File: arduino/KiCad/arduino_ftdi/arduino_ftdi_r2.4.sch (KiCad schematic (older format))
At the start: 19 parts, among them J1 RJ45, J10 9V-12V, J11 3V3 & 5V, J12 9V-12V, J13 3V3 & 5V, J2 IN/OUT, J3 DTR/TX/RX, J4 Power output 3V3, J5 NC, J6 DTR-FTDI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

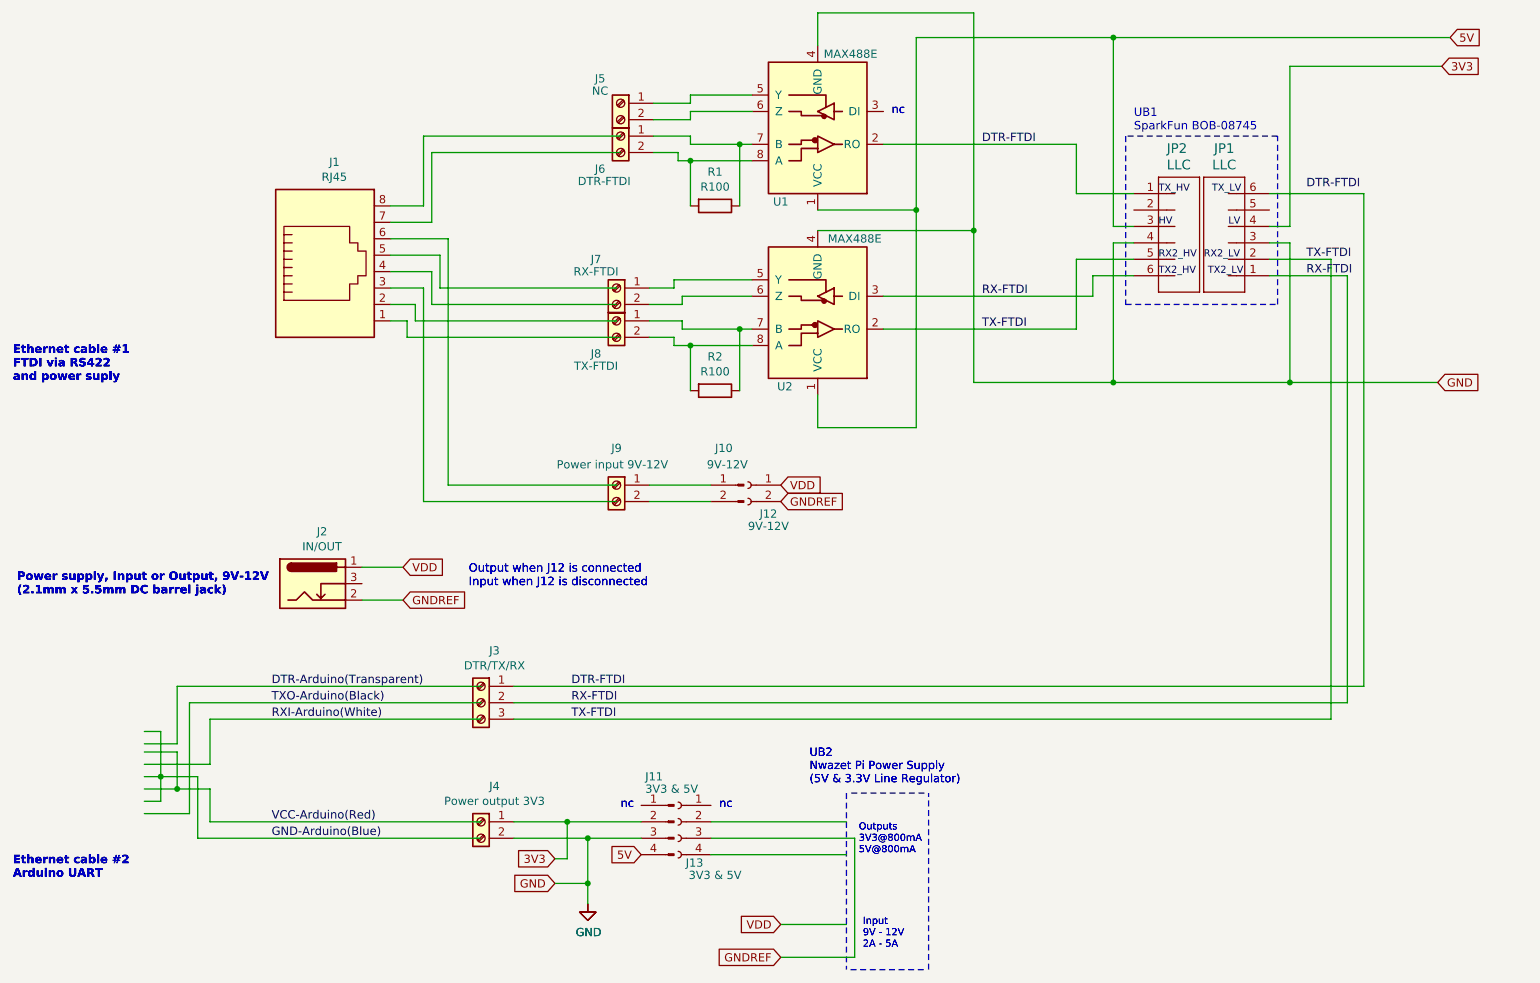
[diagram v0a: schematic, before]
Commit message: Update FTDI interface schematics
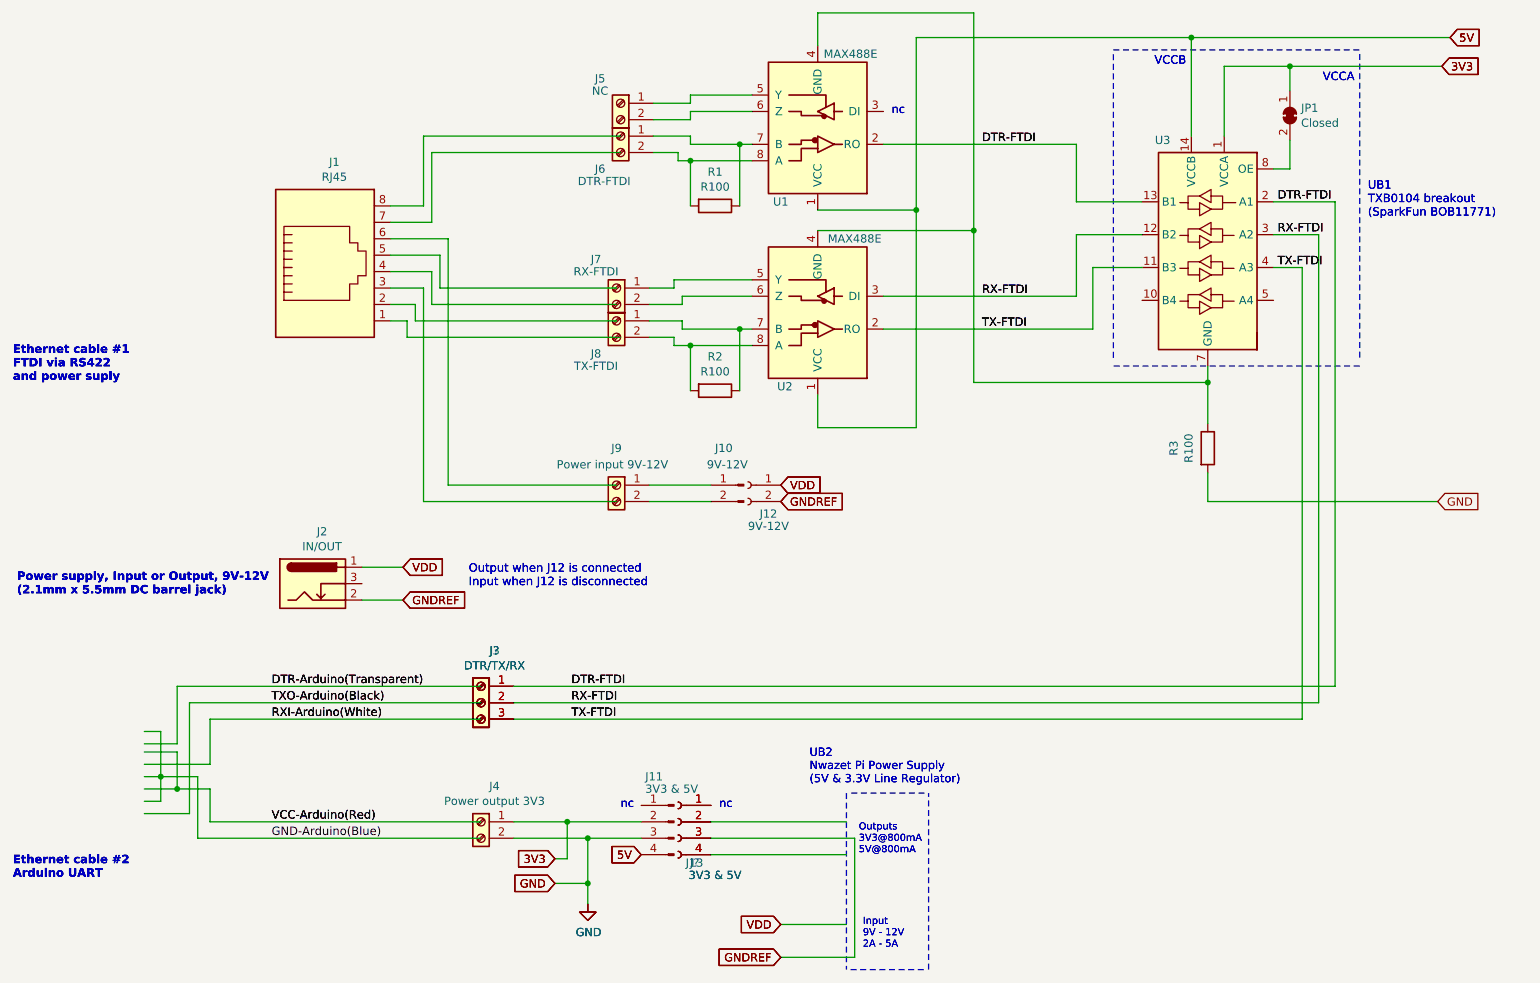
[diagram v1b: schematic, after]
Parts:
- removed JP1, JP2: LLC, symbol arduino_ftdi-eagle-import:M06SIP
- added J?: DTR/TX/RX, symbol Connector:Screw_Terminal_01x03
- added J?: 3V3 & 5V, symbol Connector:Conn_01x04_Female
- added JP1: Closed, symbol Jumper:SolderJumper_2_Bridged
- added R3: R100, symbol Device:R
- added U3: TXB0104 breakout (SparkFun BOB11771), Package_SO:SOIC-14_3.9x8.7mm_P1.27mm, symbol Logic_LevelTranslator:TXB0104D
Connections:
- net labels removed: HV, LV, RX2_HV, RX2_LV, TX2_HV, TX2_LV, TX_HV, TX_LV
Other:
- note added: "UB1\nTXB0104 breakout \n(SparkFun BOB11771)"
- note added: "VCCA"
- note added: "VCCB\n"
- note removed: "UB1\nSparkFun BOB-08745"
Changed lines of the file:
@@
 EESchema Schematic File Version 4
+LIBS:arduino_ftdi-cache
 EELAYER 30 0
 EELAYER END
@@
 Sheet 1 1
 Title "RS485 5V to UART 3V3 interface"
-Date "2021-08-21"
-Rev "3.0"
+Date "2021-04-21"
+Rev "2.4"
 Comp ""
 Comment1 "Interface to provide UART from RS485 on Ethernet cable"
@@
 Wire Wire Line
 	5250 2900 5625 2900
+$Comp
+L Logic_LevelTranslator:TXB0104D U3
+U 1 1 5F62DFF7
+P 8400 2325
+F 0 "U3" H 8675 3000 50  0000 C CNN
+F 1 "TXB0104 breakout (SparkFun BOB11771) " H 8800 1450 50  0001 C CNN
+F 2 "Package_SO:SOIC-14_3.9x8.7mm_P1.27mm" H 8400 1575 50  0001 C CNN
+F 3 "http://www.ti.com/lit/ds/symlink/txb0104.pdf" H 8510 2420 50  0001 C CNN
+	1    8400 2325
+	-1   0    0    -1
+$EndComp
 Wire Wire Line
 	6025 3400 6025 3200
@@
 	6425 1675 7600 1675
 Wire Wire Line
-	7600 1675 7600 1975
+	7600 1675 7600 2025
 Wire Wire Line
-	7600 1975 7950 1975
+	7600 2025 8000 2025
 Wire Wire Line
-	6425 2600 7700 2600
+	6425 2600 7600 2600
 Wire Wire Line
-	7700 2600 7700 2475
+	7600 2600 7600 2225
 Wire Wire Line
-	7700 2475 7950 2475
+	7600 2225 8000 2225
 Wire Wire Line
-	6425 2800 7600 2800
+	6425 2800 7700 2800
 Wire Wire Line
-	7600 2800 7600 2375
+	7700 2800 7700 2425
 Wire Wire Line
-	7600 2375 7950 2375
+	7700 2425 8000 2425
+Text GLabel 5800 3750 2    50   Input ~ 0
+VDD
 Text GLabel 5800 3850 2    50   Input ~ 0
 GNDREF
+Text GLabel 4425 6025 0    50   Input ~ 0
+3V3
 Text GLabel 4425 6175 0    50   Input ~ 0
 GND
+Text GLabel 3500 4250 2    50   Input ~ 0
+VDD
 Text GLabel 3500 4450 2    50   Input ~ 0
 GNDREF
 Wire Wire Line
 	3500 4250 3250 4250
+Text GLabel 9800 3850 2    50   Input ~ 0
+GND
+Text GLabel 9825 1200 2    50   Input ~ 0
+3V3
 Text GLabel 9875 1025 2    50   Input ~ 0
 5V
+Wire Wire Line
+	8800 1825 8900 1825
 Text GLabel 5800 6425 0    50   Input ~ 0
 VDD
@@
 Text Notes 6300 6575 0    43   ~ 0
 Input\n9V - 12V\n2A - 5A
+$Comp
+L Jumper:SolderJumper_2_Bridged JP1
+U 1 1 5F62DFF1
+P 8900 1500
+F 0 "JP1" V 8854 1568 50  0000 L CNN
+F 1 "Closed" V 8945 1568 50  0000 L CNN
+F 2 "" H 8900 1500 50  0001 C CNN
+F 3 "~" H 8900 1500 50  0001 C CNN
+	1    8900 1500
+	0    1    1    0
+$EndComp
+Wire Wire Line
+	8900 1650 8900 1825
 Text Notes 1125 6150 0    51   ~ 10
 Ethernet cable #2\nArduino UART
@@
 	5000 3850 5375 3850
 Wire Wire Line
-	7825 1025 7825 2175
-Connection ~ 7825 1025
+	8300 1025 8300 1625
+Connection ~ 8300 1025
 Wire Wire Line
 	6625 1025 6625 2075
 Wire Wire Line
+	8900 1350 8900 1200
+Connection ~ 8900 1200
+Wire Wire Line
 	6250 6625 6250 5900
 $Comp
@@
 Connection ~ 6975 2200
 Wire Wire Line
-	8775 1975 9350 1975
+	8800 2025 9175 2025
 Wire Wire Line
-	7825 1025 9875 1025
+	8800 2225 9075 2225
 Wire Wire Line
-	6625 1025 7825 1025
+	8300 1025 9875 1025
+Wire Wire Line
+	8900 1200 9825 1200
+Wire Wire Line
+	6625 1025 8300 1025
+Text GLabel 4950 6000 0    50   Input ~ 0
+5V
 Wire Wire Line
 	5375 5800 6200 5800
@@
 	4625 6175 4625 6300
 Wire Wire Line
-	8900 2175 8900 1200
+	8400 3125 8400 3375
+Wire Wire Line
+	8500 1200 8900 1200
+Wire Wire Line
+	8500 1625 8500 1200
 Text Notes 5425 5725 0    50   ~ 0
 nc
@@
 Wire Wire Line
 	3775 3750 4800 3750
+Wire Notes Line
+	9325 1125 9325 2975
+Wire Notes Line
+	9325 3025 7825 3025
+Wire Notes Line
+	7825 2975 7825 1125
+Wire Notes Line
+	7825 1100 9325 1100
+Text Notes 9375 2125 0    51   ~ 0
+UB1\nTXB0104 breakout \n(SparkFun BOB11771)
 Wire Wire Line
-	7825 2275 7825 3125
+	8400 3025 8400 3125
 Wire Wire Line
-	7825 3125 6975 3125
+	8400 3125 6975 3125
 Wire Wire Line
 	6975 2200 6975 3125
 Wire Wire Line
-	9350 1975 9350 4975
+	9175 2025 9175 4975
+Wire Wire Line
+	8800 2425 8975 2425
+Wire Wire Line
+	4175 5175 8975 5175
 Wire Wire Line
-	4175 4975 9350 4975
+	4175 4975 9175 4975
 Wire Wire Line
-	4175 5075 9250 5075
+	9075 2225 9075 5075
+Wire Wire Line
+	4175 5075 9075 5075
+Wire Wire Line
+	8975 2425 8975 5175
+Text Notes 9100 1300 0    51   ~ 0
+VCCA
+Text Notes 8075 1200 0    51   ~ 0
+VCCB\n
 Wire Wire Line
 	1925 5250 2025 5250
@@
 Text Label 2700 5075 0    51   ~ 0
 TXO-Arduino(Black)
+Text Label 2700 5175 0    51   ~ 0
+RXI-Arduino(White)
+Text Label 4525 5075 0    51   ~ 0
+RX-FTDI
 Text Label 4525 5175 0    51   ~ 0
 TX-FTDI
+Text Label 4525 4975 0    51   ~ 0
+DTR-FTDI
 $Comp
 L Connector:Screw_Terminal_01x02 J7
@@
 Text Notes 6475 1500 0    50   ~ 0
 nc
-Text Label 9000 2475 0    51   ~ 0
+Text Label 8825 2025 0    51   ~ 0
+DTR-FTDI
+Text Label 8825 2225 0    51   ~ 0
 RX-FTDI
+Text Label 8825 2425 0    51   ~ 0
+TX-FTDI
+Text Label 7025 1675 0    51   ~ 0
+DTR-FTDI
 Text Label 7025 2600 0    51   ~ 0
 RX-FTDI
 Text Label 7025 2800 0    51   ~ 0
 TX-FTDI
+$Comp
+L Connector:Screw_Terminal_01x03 J?
+U 1 1 5F5F077A
+P 3975 5075
+F 0 "J?" H 3893 5392 50  0000 C CNN
+F 1 "DTR/TX/RX" H 3893 5301 50  0000 C CNN
+F 2 "" H 3975 5075 50  0001 C CNN
+F 3 "~" H 3975 5075 50  0001 C CNN
+	1    3975 5075
+	-1   0    0    -1
+$EndComp
+$Comp
+L Connector:Conn_01x04_Female J?
+U 1 1 5F60BAA6
+P 5175 5800
+F 0 "J?" H 5075 5550 50  0000 C CNN
+F 1 "3V3 & 5V" H 4950 5475 50  0000 C CNN
+F 2 "" H 5175 5800 50  0001 C CNN
+F 3 "~" H 5175 5800 50  0001 C CNN
+	1    5175 5800
+	-1   0    0    -1
+$EndComp
 Text GLabel 5800 3750 2    50   Input ~ 0
 VDD
+Text GLabel 5800 3850 2    50   Input ~ 0
+GNDREF
 Text GLabel 4425 6025 0    50   Input ~ 0
 3V3
+Text GLabel 4425 6175 0    50   Input ~ 0
+GND
 Text GLabel 3500 4250 2    50   Input ~ 0
 VDD
+Text GLabel 3500 4450 2    50   Input ~ 0
+GNDREF
 Text GLabel 9825 1200 2    50   Input ~ 0
 3V3
+Text GLabel 9875 1025 2    50   Input ~ 0
+5V
+Text GLabel 5800 6425 0    50   Input ~ 0
+VDD
+Text GLabel 5800 6625 0    50   Input ~ 0
+GNDREF
 Text Notes 5975 5575 0    50   ~ 0
 UB2\nNwazet Pi Power Supply\n(5V & 3.3V Line Regulator)
@@
 EndData
 $EndBitmap
+Text Notes 9375 2125 0    51   ~ 0
+UB1\nTXB0104 breakout \n(SparkFun BOB11771)
+Text Notes 9100 1300 0    51   ~ 0
+VCCA
+Text Notes 8075 1200 0    51   ~ 0
+VCCB\n
+Text Label 2700 5800 0    51   ~ 0
+VCC-Arduino(Red)
+Text Label 2700 5900 0    51   ~ 0
+GND-Arduino(Blue)
+Text Label 2700 4975 0    51   ~ 0
+DTR-Arduino(Transparent)
+Text Label 2700 5075 0    51   ~ 0
+TXO-Arduino(Black)
 Text Label 2700 5175 0    51   ~ 0
 RXI-Arduino(White)
 Text Label 4525 5075 0    51   ~ 0
 RX-FTDI
+Text Label 4525 5175 0    51   ~ 0
+TX-FTDI
 Text Label 4525 4975 0    51   ~ 0
 DTR-FTDI
 Text Notes 6475 1500 0    50   ~ 0
 nc
+Text Label 8825 2025 0    51   ~ 0
+DTR-FTDI
+Text Label 8825 2225 0    51   ~ 0
+RX-FTDI
+Text Label 8825 2425 0    51   ~ 0
+TX-FTDI
 Text Label 7025 1675 0    51   ~ 0
 DTR-FTDI
+Text Label 7025 2600 0    51   ~ 0
+RX-FTDI
+Text Label 7025 2800 0    51   ~ 0
+TX-FTDI
 Wire Wire Line
 	5250 1475 5625 1475
@@
 Wire Wire Line
 	5150 2500 5625 2500
-Connection ~ 7825 3125
-Wire Wire Line
-	7825 3125 8900 3125
-Text GLabel 9800 3125 2    50   Input ~ 0
-GND
-Wire Wire Line
-	8900 1200 9825 1200
 $Comp
-L arduino_ftdi-eagle-import:M06SIP JP1
-U 1 1 612696AD
-P 8575 2275
-F 0 "JP1" H 8500 2850 59  0000 C CNN
-F 1 "LLC" H 8500 2750 59  0000 C CNN
-F 2 "" H 8575 2275 51  0001 C CNN
-F 3 "" H 8575 2275 51  0001 C CNN
-	1    8575 2275
+L Device:R R3
+U 1 1 6080F85B
+P 8400 3525
+F 0 "R3" V 8193 3525 50  0000 C CNN
+F 1 "R100" V 8284 3525 50  0000 C CNN
+F 2 "" V 8330 3525 50  0001 C CNN
+F 3 "~" H 8400 3525 50  0001 C CNN
+	1    8400 3525
 	1    0    0    -1
 $EndComp
-$Comp
-L arduino_ftdi-eagle-import:M06SIP JP2
-U 1 1 61271DCC
-P 8150 2175
-F 0 "JP2" H 8150 1700 59  0000 R CNN
-F 1 "LLC" H 8150 1800 59  0000 R CNN
-F 2 "" H 8150 2175 51  0001 C CNN
-F 3 "" H 8150 2175 51  0001 C CNN
-	1    8150 2175
-	-1   0    0    1
-$EndComp
-Text Label 8100 1975 0    43   ~ 0
-TX_HV
-Text Notes 7950 1600 0    51   ~ 0
-UB1\nSparkFun BOB-08745
-Wire Wire Line
-	4175 5175 9150 5175
-Wire Wire Line
-	9250 2475 9250 5075
-Wire Wire Line
-	8775 2475 9250 2475
-Wire Wire Line
-	9150 2375 9150 5175
-Wire Wire Line
-	8775 2375 9150 2375
-Text Label 8425 1975 0    43   ~ 0
-TX_LV
-Text Label 8100 2475 0    43   ~ 0
-TX2_HV
-Text Label 8400 2475 0    43   ~ 0
-TX2_LV
-Text Label 8100 2375 0    43   ~ 0
-RX2_HV
-Text Label 8375 2375 0    43   ~ 0
-RX2_LV
-Wire Wire Line
-	7825 2175 7950 2175
-Text Label 8100 2175 0    43   ~ 0
-HV
-Text Label 8525 2175 0    43   ~ 0
-LV
-Wire Wire Line
-	8900 2175 8775 2175
-Wire Notes Line
-	7900 1625 7900 2650
-Wire Notes Line
-	7900 2650 8825 2650
-Wire Notes Line
-	8825 2650 8825 1625
-Wire Notes Line
-	8825 1625 7900 1625
+Connection ~ 8400 3125
 Wire Wire Line
-	7825 2275 7950 2275
+	8400 3675 8400 3850
 Wire Wire Line
-	8775 2275 8900 2275
-Wire Wire Line
-	8900 2275 8900 3125
-Connection ~ 8900 3125
-Wire Wire Line
-	8900 3125 9800 3125
-Text Label 9000 1950 0    51   ~ 0
-DTR-FTDI
-Text Label 9000 2375 0    51   ~ 0
-TX-FTDI
-Text Label 2700 5900 0    51   ~ 0
-GND-Arduino(Blue)
+	8400 3850 9800 3850
 $EndSCHEMATC
